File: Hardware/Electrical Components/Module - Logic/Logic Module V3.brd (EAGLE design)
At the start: 70.5 x 70 mm, 16 parts

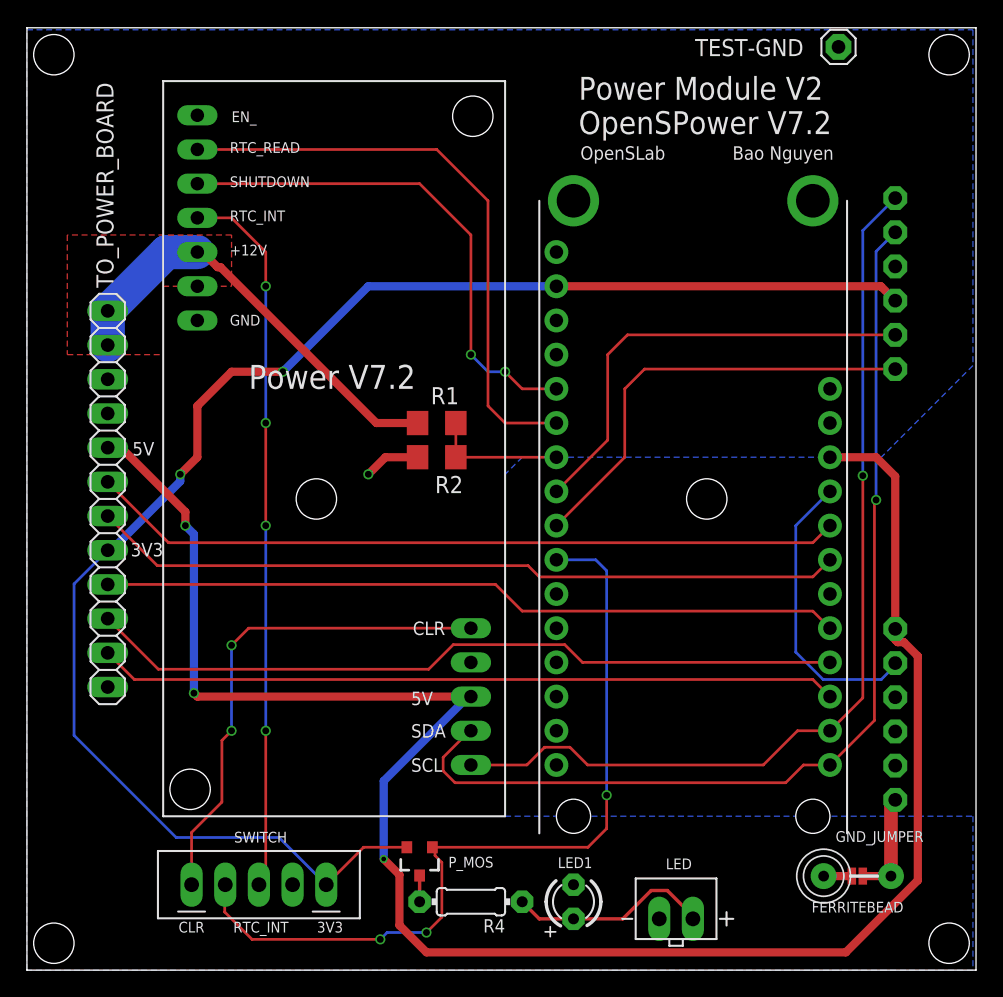
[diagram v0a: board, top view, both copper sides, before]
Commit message: First draft for Logic Module V3
Combine Power V7.3 with Logic Module
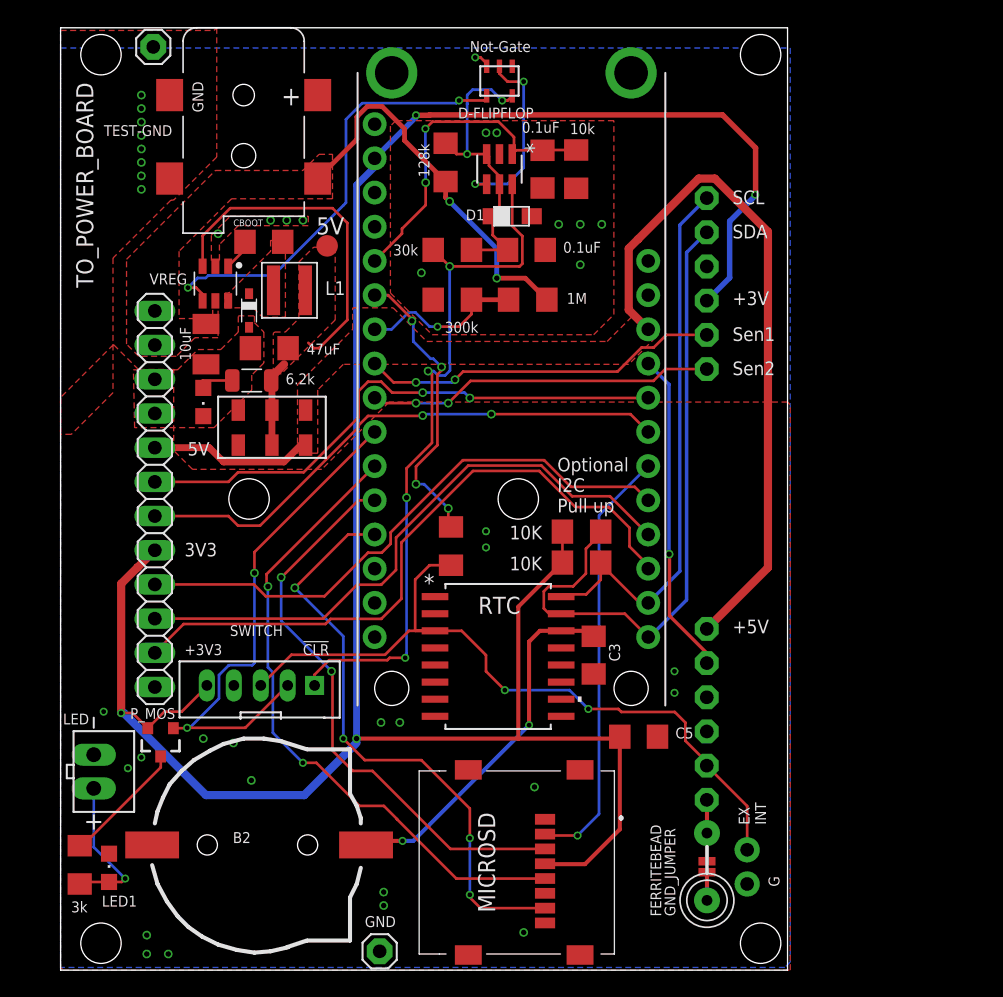
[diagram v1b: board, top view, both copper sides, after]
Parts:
- added 12V_IN: 2.1MMJACKSMT, adafruit:DCJACK_2MM_SMT
- added 5V: TPTP16R, testpad:TP16R
- added B2: cr1220, microbuilder:CR1220-2
- added C1, C2, C3: 0.1uF, adafruit:C1206
- added C5: 100nF, resistor:C1206
- added CBOOT: 100nF, rcl:C1206
- added CIN: 10uF, rcl:C1206K
- added COUT: 47uF, rcl:C1206
- added D-FLIPFLOP: SN74LVC1G175DBVR, eDNA:DBV6
- added D1: 4.3V, beach:DO-219AC
- added D3: NSR0320MW2T1G, diode:SOD323_ST
- added EXTERNAL_INT: (no value), SparkFun-Connectors:1X02_NO_SILK
- added L1: 10UH 2.7A, EMCComponents (rev19e):WE-MAPI_40XX
- added LED2: RED, adafruit:CHIPLED_0805
- added MICROSD: 47219-2001, SamacSys_Parts:472192001
- added R10, R7: 30k, adafruit:R1206
- added R11: 6.2k, Resistor_Capacitor:RES_1206
- added R3, R5: 10K, rcl:R1206
- added R6: 128k, adafruit:R1206
- added R8: 10k, adafruit:R1206
- added RTC: DS3231SNT&R, eDNA:21-0042B_16
- added TEST-GND1: (no value), adafruit:1X01
- added U$3: NOT_GATE, eDNA:SOT753
- added VREG: BUCK_REGULATORS, eDNA:SOT23-6
- LED1: value Orange -> Yellow; device adafruit:LED3MM -> adafruit:CHIPLED_0805
- R4: value 200 -> 3k; device adafruit:0204/7 -> resistor:R1206
- SWITCH: value 2.5MM_JST_UP_5POS -> 2MM_JST_PH_5POS; device eDNA:JST_5POS_2.5MM_UP -> eDNA:2MM_5POS_HEADER
- U$1: value OPENS_POWER_7.2 -> 2PDT_SWITCHJS-SMD; device eDNA:OPENS_POWER_7.2 -> eDNA:JS-DPDT-SMD
- moved TEST-GND 50.9 mm to (6.88, 68.6)
- moved LED 44.6 mm to (2.46, 14.8), turned to 270 degrees
- moved LED1 34.6 mm to (3.60, 7.60), turned to 0 degrees
- moved U$1 32.0 mm to (18.2, 41.6), turned to 180 degrees
- moved U$2 30.2 mm to (43.9, 6.09)
- moved R4 29.2 mm to (1.42, 7.82), turned to 90 degrees
- moved P_MOS 21.2 mm to (7.43, 17.0)
- moved MS1 16.5 mm to (22.1, 69.2)
- moved SWITCH 14.8 mm to (14.9, 21.1), turned to 180 degrees
- moved TO_SENSOR_BOARD1 14.0 mm to (48.0, 51.0)
- moved TO_SENSOR_BOARD2 14.0 mm to (48.0, 19.0)
- moved R2 11.8 mm to (29.1, 49.8)
- moved R1 11.4 mm to (34.7, 49.8), turned to 0 degrees
- moved FERRITEBEAD 11.2 mm to (48.0, 7.68), turned to 270 degrees
- moved GND_JUMPER 11.2 mm to (48.0, 7.68), turned to 90 degrees
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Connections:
- removed net SD_CS: MS1.22
- new net !EN: D-FLIPFLOP.4, U$3.2
- new net 2.2VCC: C1.1, D-FLIPFLOP.3, D-FLIPFLOP.5, D1.FNT, R6.1, R7.2, U$3.5
- new net 5VUSB: 5V.TP, COUT.1, L1.2, R11.2, U$1.P$2, U$1.P$5, VREG.3
- new net CS: MICROSD.2, MS1.22
- new net DI: MICROSD.3, MS1.12
- new net DO: MICROSD.7, MS1.13
- new net EN: U$3.4, VREG.4
- new net N$1: B2.+, C3.1, RTC.14
- new net N$12: LED2.A, R11.1
- new net N$16: CBOOT.1, VREG.1
- new net N$17: CBOOT.2, D3.C, L1.1, VREG.6
- new net SCK: MICROSD.5, MS1.11
- net !CLR: now also D-FLIPFLOP.6, R7.1; no longer U$1.8
- net +12V: now also 12V_IN.PWR2, CIN.1, R6.2, VREG.5; no longer U$1.5
- net +3V3: now also C5.1, MICROSD.4, R3.2, R5.2
- net +5V: now also U$1.P$1, U$1.P$4; no longer U$1.10
- net GND: now also 12V_IN.GND, 12V_IN.GNDBREAK, B2.-, C1.2, C2.1, C3.2, C5.2, CIN.2, COUT.2, D-FLIPFLOP.2, D1.BCK, D3.A, EXTERNAL_INT.1, LED1.C, LED2.C, MICROSD.10, MICROSD.11, MICROSD.12, MICROSD.6, MICROSD.9, R8.1, RTC.10, RTC.11, RTC.12, RTC.13, RTC.2, RTC.5, RTC.6, RTC.7, RTC.8, RTC.9, TEST-GND1.1, U$3.3, VREG.2; no longer LED1.K, U$1.7
- net RTC_INT: now also EXTERNAL_INT.2, R10.2, RTC.3, TO_SENSOR_BOARD2.5; no longer U$1.4
- net RTC_READ: now also R10.1; no longer U$1.2
- net SCL: now also R3.1, RTC.16; no longer U$1.12
- net SDA: now also R5.1, RTC.15; no longer U$1.11
- net SHUTDOWN: now also C2.2, D-FLIPFLOP.1, R8.2; no longer U$1.3
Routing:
- net +5V: track 140.4 -> 64.3 mm, vias 3 -> 0
- net +3V3: track 114.8 -> 180.4 mm, vias 2 -> 4
- net SCK: track 0.00 -> 48.0 mm, vias 0 -> 2
- net DO: track 0.00 -> 44.3 mm, vias 0 -> 4
- net DI: track 0.00 -> 42.6 mm, vias 0 -> 2
- net EN: track 0.00 -> 33.6 mm, vias 0 -> 2
- net 5VUSB: track 0.00 -> 32.5 mm
- net CS: track 0.00 -> 32.1 mm, vias 0 -> 1
- net SCL: track 70.4 -> 41.4 mm, vias 1 -> 0
- net N$1: track 0.00 -> 27.3 mm, vias 0 -> 2
- net SDA: track 75.1 -> 49.2 mm, vias 1 -> 0
- net WAKE_NOSLEEP: track 61.9 -> 38.7 mm, vias 3 -> 2
- net 2.2VCC: track 0.00 -> 22.6 mm, vias 0 -> 2
- net RTC_READ: track 44.0 -> 22.2 mm, vias 0 -> 4
- net !CLR: track 37.3 -> 53.4 mm, vias 2 -> 4
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- added copper zone on layer 1, net +5V
- added copper zone on layer 1, net 5VUSB
- added copper zone on layer 1, net GND
- added copper zone on layer 1, net N$17
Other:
- board size 70.5 x 70 mm -> 54 x 70 mm
- board text added: "!CLR"
- board text added: "+3V"
- board text added: "EX INT"
- board text added: "G"
- board text added: "Kawin Pechetratanapanit"
- board text added: "Not-Gate"
- board text added: "OPEnSLab"
- board text added: "Optional I2C Pull up"
- board text added: "Power Module V3 OpenSPower V7.3"
- board text added: "Sen1"
- board text added: "Sen2"
- board text added: "Shift_Ck"
- board text added: "Shift_D"
- board text added: "Shift_L"
- board text removed: "CLR"
- board text removed: "EN_"
- board text removed: "OpenSLab"
- board text removed: "Power Module V2 OpenSPower V7.2"
- board text removed: "RTC_INT"
- board text removed: "RTC_READ"
- board text removed: "SHUTDOWN"
- board text removed: "Shift_Clk"
- board text removed: "Shift_Data"
- board text removed: "Shift_Latch"
- board text removed: "TEST_GND"
